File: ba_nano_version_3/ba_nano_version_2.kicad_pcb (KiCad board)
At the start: 2 copper layers, 71.3 x 98 mm, 84 parts, among them J1 GPIO_0, J2 GPIO_1, Q1 2N3904, Q2 2N3904, SW1 , SW10 , SW11 , SW12 , SW13 , SW14 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

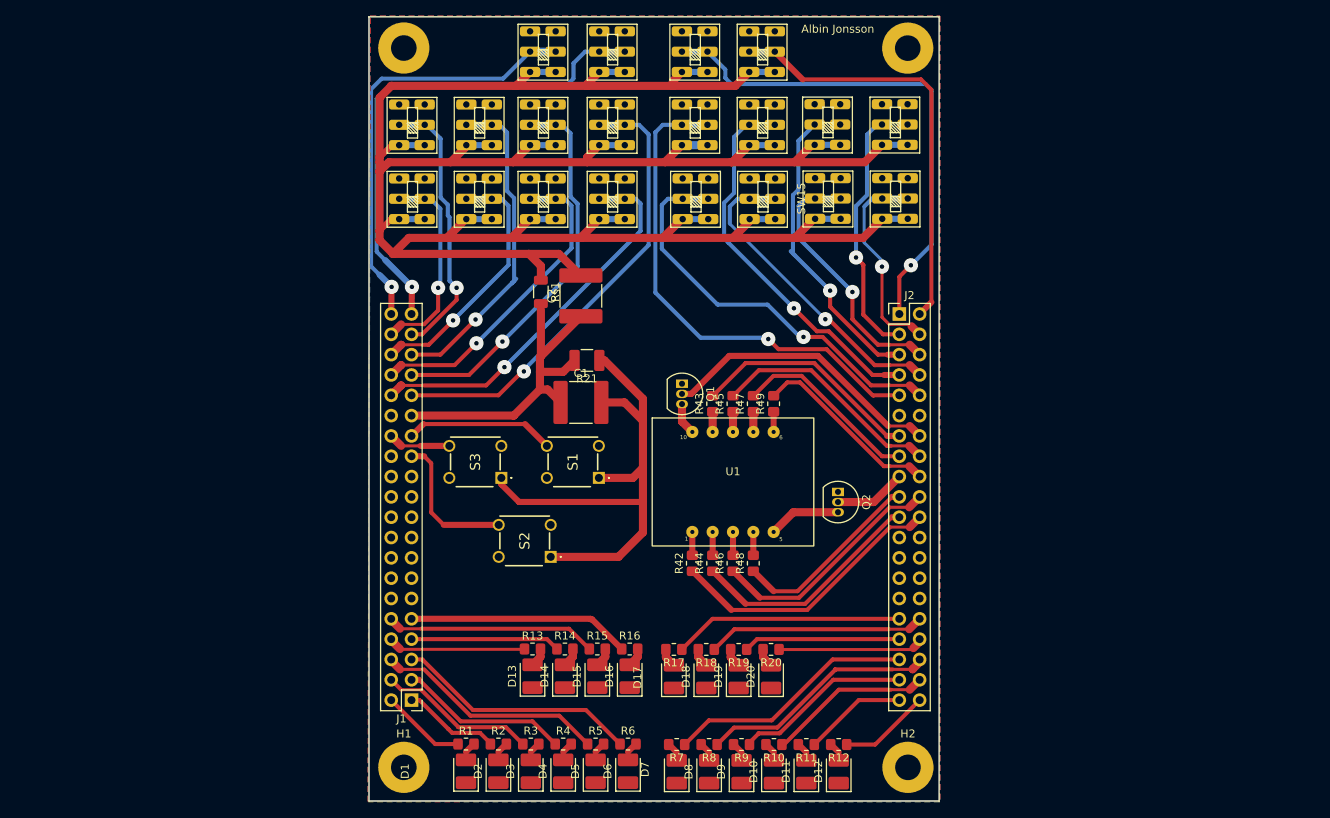
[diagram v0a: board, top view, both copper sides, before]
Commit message: Made changes to KiCad schematic and CAD drawing. Changed SSDs and buttons
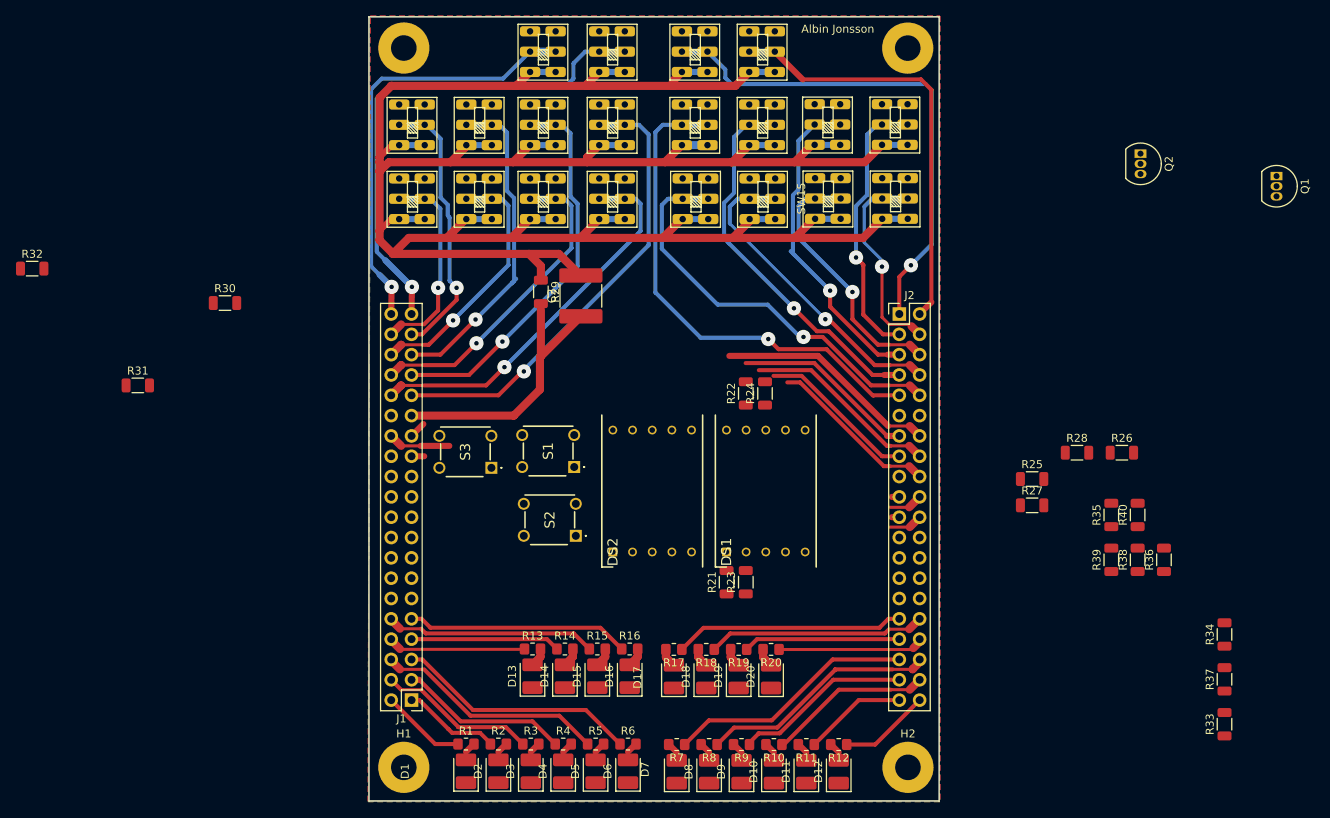
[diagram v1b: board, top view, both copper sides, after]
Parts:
- removed C1: 1, Capacitor_SMD:C_2220_5650Metric
- removed R42, R43, R44, R45, R46, R47, R48, R49: 150, Resistor_SMD:R_0805_2012Metric_Pad1.20x1.40mm_HandSolder
- removed U1: ELD-425SYGWA, Old_KiCad_footprints:ELD-425SYGWA
- added DS1: LS0565SRWK, Old_KiCad_footprints:LS0565SRWK, F.Cu at (143.6, 119.4)
- added DS2: LS0565SRWK, Old_KiCad_footprints:LS0565SRWK, F.Cu at (129.4, 119.4)
- added R22: 82, Resistor_SMD:R_1206_3216Metric, F.Cu at (146.0, 99.5)
- added R23: 82, Resistor_SMD:R_1206_3216Metric, F.Cu at (146.0, 123.2)
- added R24: 82, Resistor_SMD:R_1206_3216Metric, F.Cu at (148.4, 99.5)
- added R25: 82, Resistor_SMD:R_1206_3216Metric, F.Cu at (181.8, 110.2)
- added R26: 82, Resistor_SMD:R_1206_3216Metric, F.Cu at (193.0, 107.0)
- added R27: 82, Resistor_SMD:R_1206_3216Metric, F.Cu at (181.8, 113.5)
- added R28: 82, Resistor_SMD:R_1206_3216Metric, F.Cu at (187.4, 107.0)
- added R30: 680, Resistor_SMD:R_1206_3216Metric, F.Cu at (80.9, 88.2)
- added R31: 680, Resistor_SMD:R_1206_3216Metric, F.Cu at (70.0, 98.5)
- added R32: 680, Resistor_SMD:R_1206_3216Metric, F.Cu at (56.8, 84.0)
- added R33: 82, Resistor_SMD:R_1206_3216Metric, F.Cu at (205.8, 140.9)
- added R34: 82, Resistor_SMD:R_1206_3216Metric, F.Cu at (205.8, 129.7)
- added R35: 82, Resistor_SMD:R_1206_3216Metric, F.Cu at (191.7, 114.7)
- added R36: 82, Resistor_SMD:R_1206_3216Metric, F.Cu at (198.3, 120.3)
- added R37: 82, Resistor_SMD:R_1206_3216Metric, F.Cu at (205.8, 135.3)
- added R38: 82, Resistor_SMD:R_1206_3216Metric, F.Cu at (195.0, 120.3)
- added R39: 82, Resistor_SMD:R_1206_3216Metric, F.Cu at (191.7, 120.3)
- added R40: 82, Resistor_SMD:R_1206_3216Metric, F.Cu at (195.0, 114.7)
- R21: footprint Resistor_SMD:R_1210_3225Metric_Pad1.30x2.65mm_HandSolder -> Resistor_SMD:R_1206_3216Metric
- moved Q1 78.7 mm to (212.3, 72.4)
- moved Q2 56.7 mm to (195.3, 69.6)
- moved R21 32.8 mm to (143.6, 123.2), turned to 90 degrees
- moved S2 4.09 mm to (124.8, 117.3)
- moved S1 3.37 mm to (124.5, 108.8)
- moved S3 1.77 mm to (114.2, 108.8)
- renumbered R§1 to R29
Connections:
- Q1 pad 2: /GPIO_1_13 -> /GPIO_0_13
- R21 pad 1: Net-(S1-Pad1) -> /GPIO_1_21
- R21 pad 2: +3V3 -> Net-(DS1-Pad1)
- S1 pad 1: Net-(S1-Pad1) -> +3V3
- S1 pad 2: Net-(S1-Pad1) -> +3V3
- S2 pad 1: Net-(S1-Pad1) -> +3V3
- S2 pad 2: Net-(S1-Pad1) -> +3V3
- S3 pad 1: Net-(S1-Pad1) -> +3V3
- S3 pad 2: Net-(S1-Pad1) -> +3V3
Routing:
- net Net-(S1-Pad1): track 68.8 -> 0.00 mm
- net /GPIO_1_21: track 35.2 -> 4.22 mm
- net /GPIO_1_20: track 29.5 -> 0.94 mm
- net /GPIO_1_19: track 29.9 -> 4.30 mm
- net /GPIO_1_18: track 24.2 -> 0.92 mm
- net /GPIO_0_26: track 18.7 -> 2.10 mm
- net /GPIO_0_24: track 18.1 -> 1.59 mm
- net Net-(Q2-Pad3): track 9.07 -> 0.00 mm
- net /GPIO_1_16: track 8.98 -> 0.00 mm
- net +3V3: track 42.8 -> 34.7 mm
- net /GPIO_1_13: track 35.8 -> 27.9 mm
- net /GPIO_1_12: track 28.8 -> 23.0 mm
- net /GPIO_1_15: track 29.1 -> 24.6 mm
- net Net-(Q1-Pad3): track 4.02 -> 0.00 mm
- net /GPIO_1_14: track 23.5 -> 19.9 mm
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
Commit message: Completed the adding of buttons and two independetely controlled SSDs
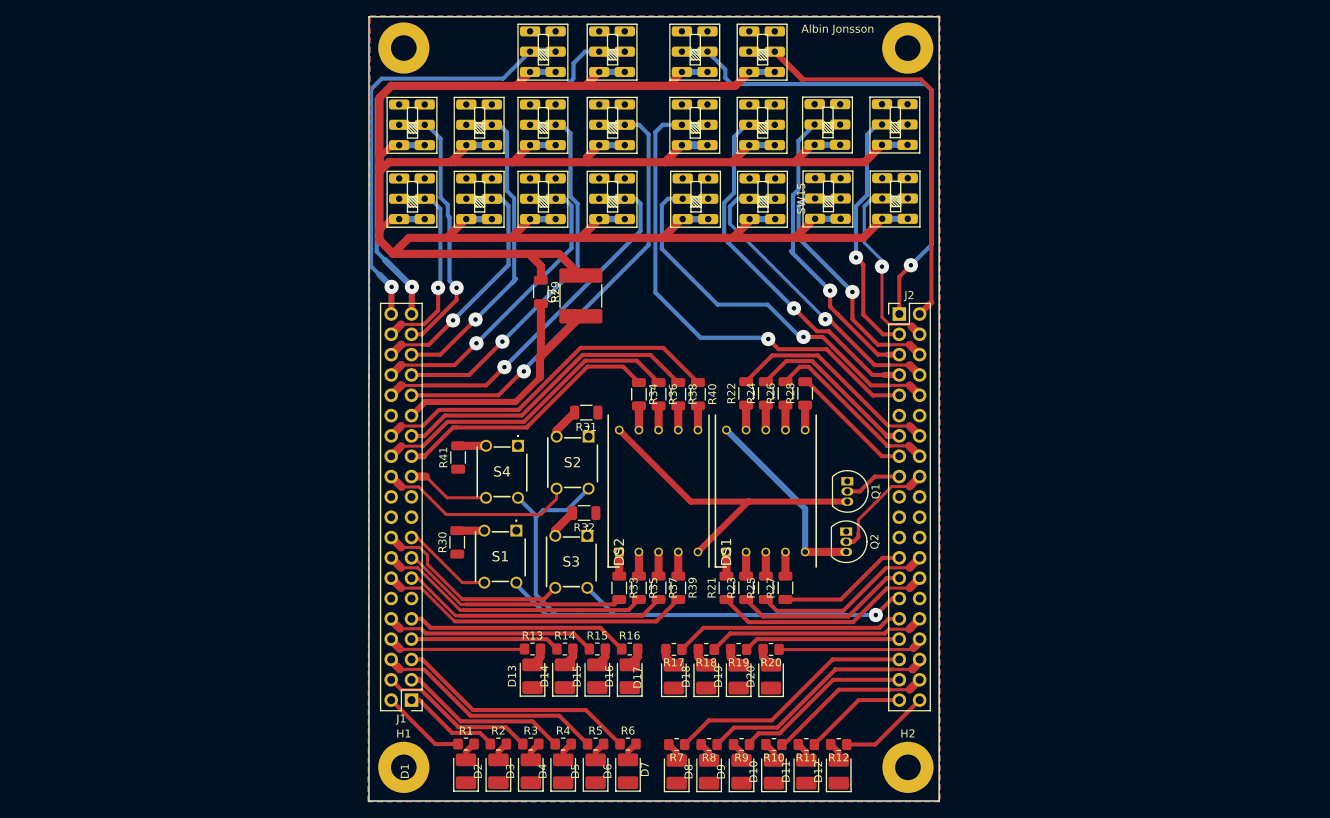
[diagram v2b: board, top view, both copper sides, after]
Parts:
- added R41: 680, Resistor_SMD:R_1206_3216Metric, F.Cu at (110.0, 107.6)
- added S4: CB15FP, CB15FP:CB15FP, F.Cu at (117.5, 106.1)
- moved R34 79.1 mm to (132.6, 99.6), turned to -90 degrees
- moved R33 77.6 mm to (130.2, 123.8), turned to -90 degrees
- moved R32 75.5 mm to (125.8, 114.5), turned to 180 degrees
- moved R37 71.7 mm to (135.1, 123.8), turned to -90 degrees
- moved R36 66.5 mm to (135.1, 99.6), turned to -90 degrees
- moved Q1 65.8 mm to (158.7, 110.5)
- moved R38 61.0 mm to (137.6, 99.6), turned to -90 degrees
- moved Q2 59.9 mm to (158.6, 116.8)
- moved R35 59.7 mm to (132.6, 123.8), turned to -90 degrees
- moved R40 57.0 mm to (140.0, 99.6), turned to -90 degrees
- moved R31 56.2 mm to (126.0, 102.0), turned to 180 degrees
- moved R39 54.2 mm to (137.6, 123.8), turned to -90 degrees
- moved R26 42.7 mm to (151.0, 99.5), turned to 90 degrees
- moved R30 41.7 mm to (109.9, 118.2), turned to 90 degrees
- moved R25 36.0 mm to (148.5, 123.8), turned to 90 degrees
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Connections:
- Q1 pad 2: /GPIO_0_13 -> /GPIO_1_16
- Q2 pad 2: /GPIO_1_16 -> /GPIO_1_17
- R21 pad 1: /GPIO_1_21 -> /GPIO_1_27
- R22 pad 2: /GPIO_1_12 -> /GPIO_1_13
- R23 pad 1: /GPIO_1_20 -> /GPIO_1_26
- R24 pad 2: /GPIO_1_15 -> /GPIO_1_12
- R25 pad 1: /GPIO_1_19 -> /GPIO_1_25
- R26 pad 2: /GPIO_1_14 -> /GPIO_1_15
- R27 pad 1: /GPIO_1_18 -> /GPIO_1_24
- R28 pad 2: /GPIO_1_17 -> /GPIO_1_14
- R30 pad 2: /GPIO_0_26 -> /GPIO_0_16
- R31 pad 2: /GPIO_0_24 -> /GPIO_0_23
- R32 pad 2: /GPIO_0_27 -> /GPIO_0_17
- R33 pad 2: /GPIO_0_17 -> /GPIO_0_14
- R34 pad 1: /GPIO_0_18 -> /GPIO_0_24
- R35 pad 2: /GPIO_0_14 -> /GPIO_0_15
- R36 pad 1: /GPIO_0_19 -> /GPIO_0_25
- R37 pad 2: /GPIO_0_15 -> /GPIO_0_12
- R38 pad 1: /GPIO_0_20 -> /GPIO_0_26
- R39 pad 2: /GPIO_0_12 -> /GPIO_0_13
- R40 pad 1: /GPIO_0_21 -> /GPIO_0_27
- S1 pad 3: /GPIO_0_26 -> /GPIO_0_16
- S1 pad 4: /GPIO_0_26 -> /GPIO_0_16
- S2 pad 3: /GPIO_0_24 -> /GPIO_0_23
- S2 pad 4: /GPIO_0_24 -> /GPIO_0_23
- S3 pad 3: /GPIO_0_27 -> /GPIO_0_17
- S3 pad 4: /GPIO_0_27 -> /GPIO_0_17
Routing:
- net +3V3: track 34.7 -> 115.3 mm, vias 0 -> 1
- net Net-(DS2-Pad10): track 0.00 -> 41.2 mm
- net /GPIO_0_25: track 0.00 -> 39.5 mm
- net /GPIO_0_13: track 0.00 -> 39.3 mm
- net /GPIO_0_27: track 7.78 -> 44.7 mm
- net /GPIO_0_26: track 2.10 -> 38.9 mm
- net /GPIO_0_15: track 0.00 -> 34.3 mm
- net /GPIO_0_12: track 0.00 -> 33.7 mm
- net /GPIO_0_24: track 1.59 -> 33.9 mm
- net /GPIO_0_17: track 0.00 -> 28.7 mm
- net /GPIO_0_23: track 0.00 -> 28.7 mm
- net /GPIO_0_14: track 0.00 -> 28.6 mm
- net /GPIO_1_27: track 0.00 -> 27.6 mm
- net Net-(DS1-Pad10): track 0.00 -> 24.5 mm
- net /GPIO_1_25: track 0.00 -> 22.6 mm
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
